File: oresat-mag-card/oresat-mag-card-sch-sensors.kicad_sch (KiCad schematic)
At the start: 22 parts, among them U10 LTC4300A-1, U11 MAX892LEUA+T, U9 ICM-42688-P

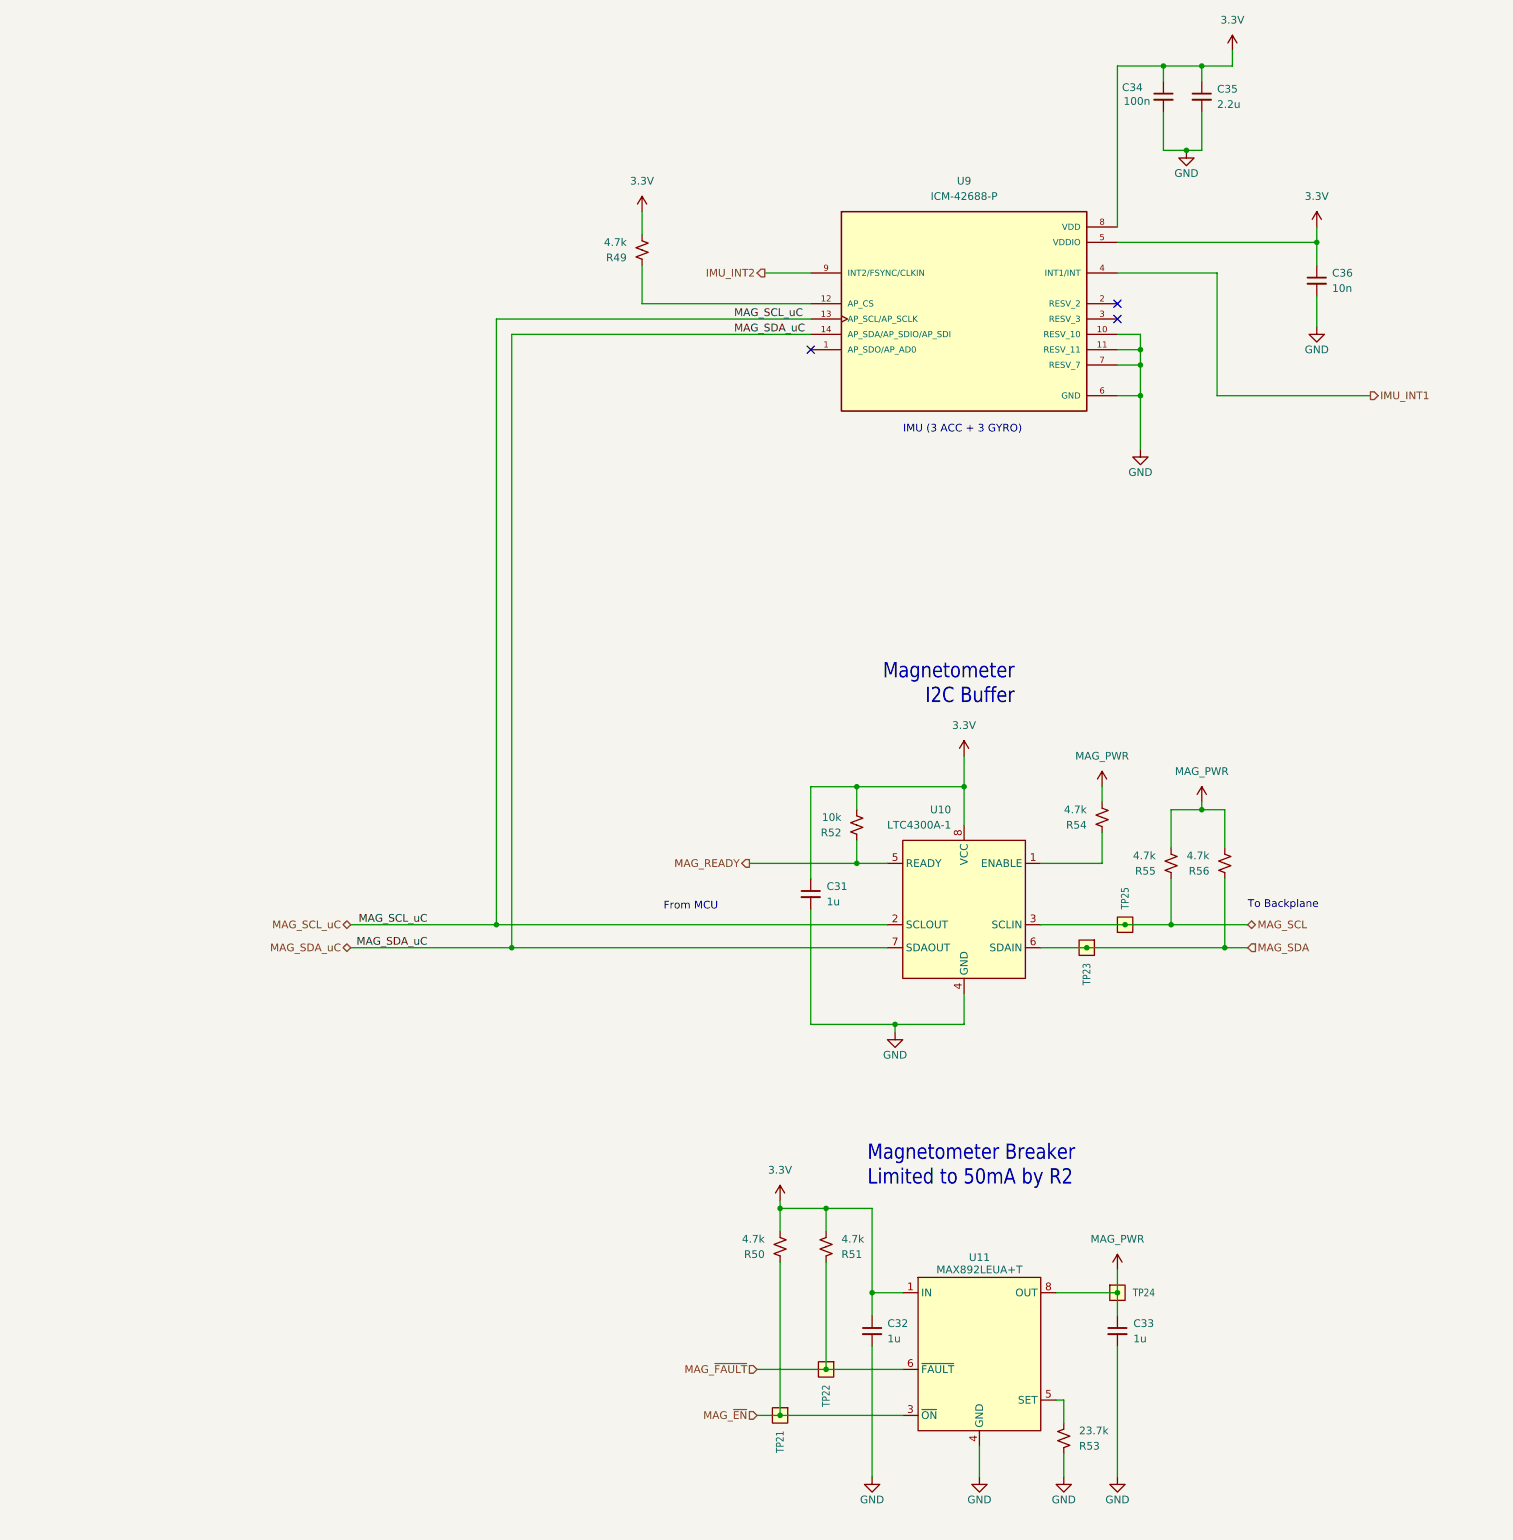
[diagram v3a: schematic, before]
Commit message: Schematic polish, fixed UART TX/RX mixup, imported into layout
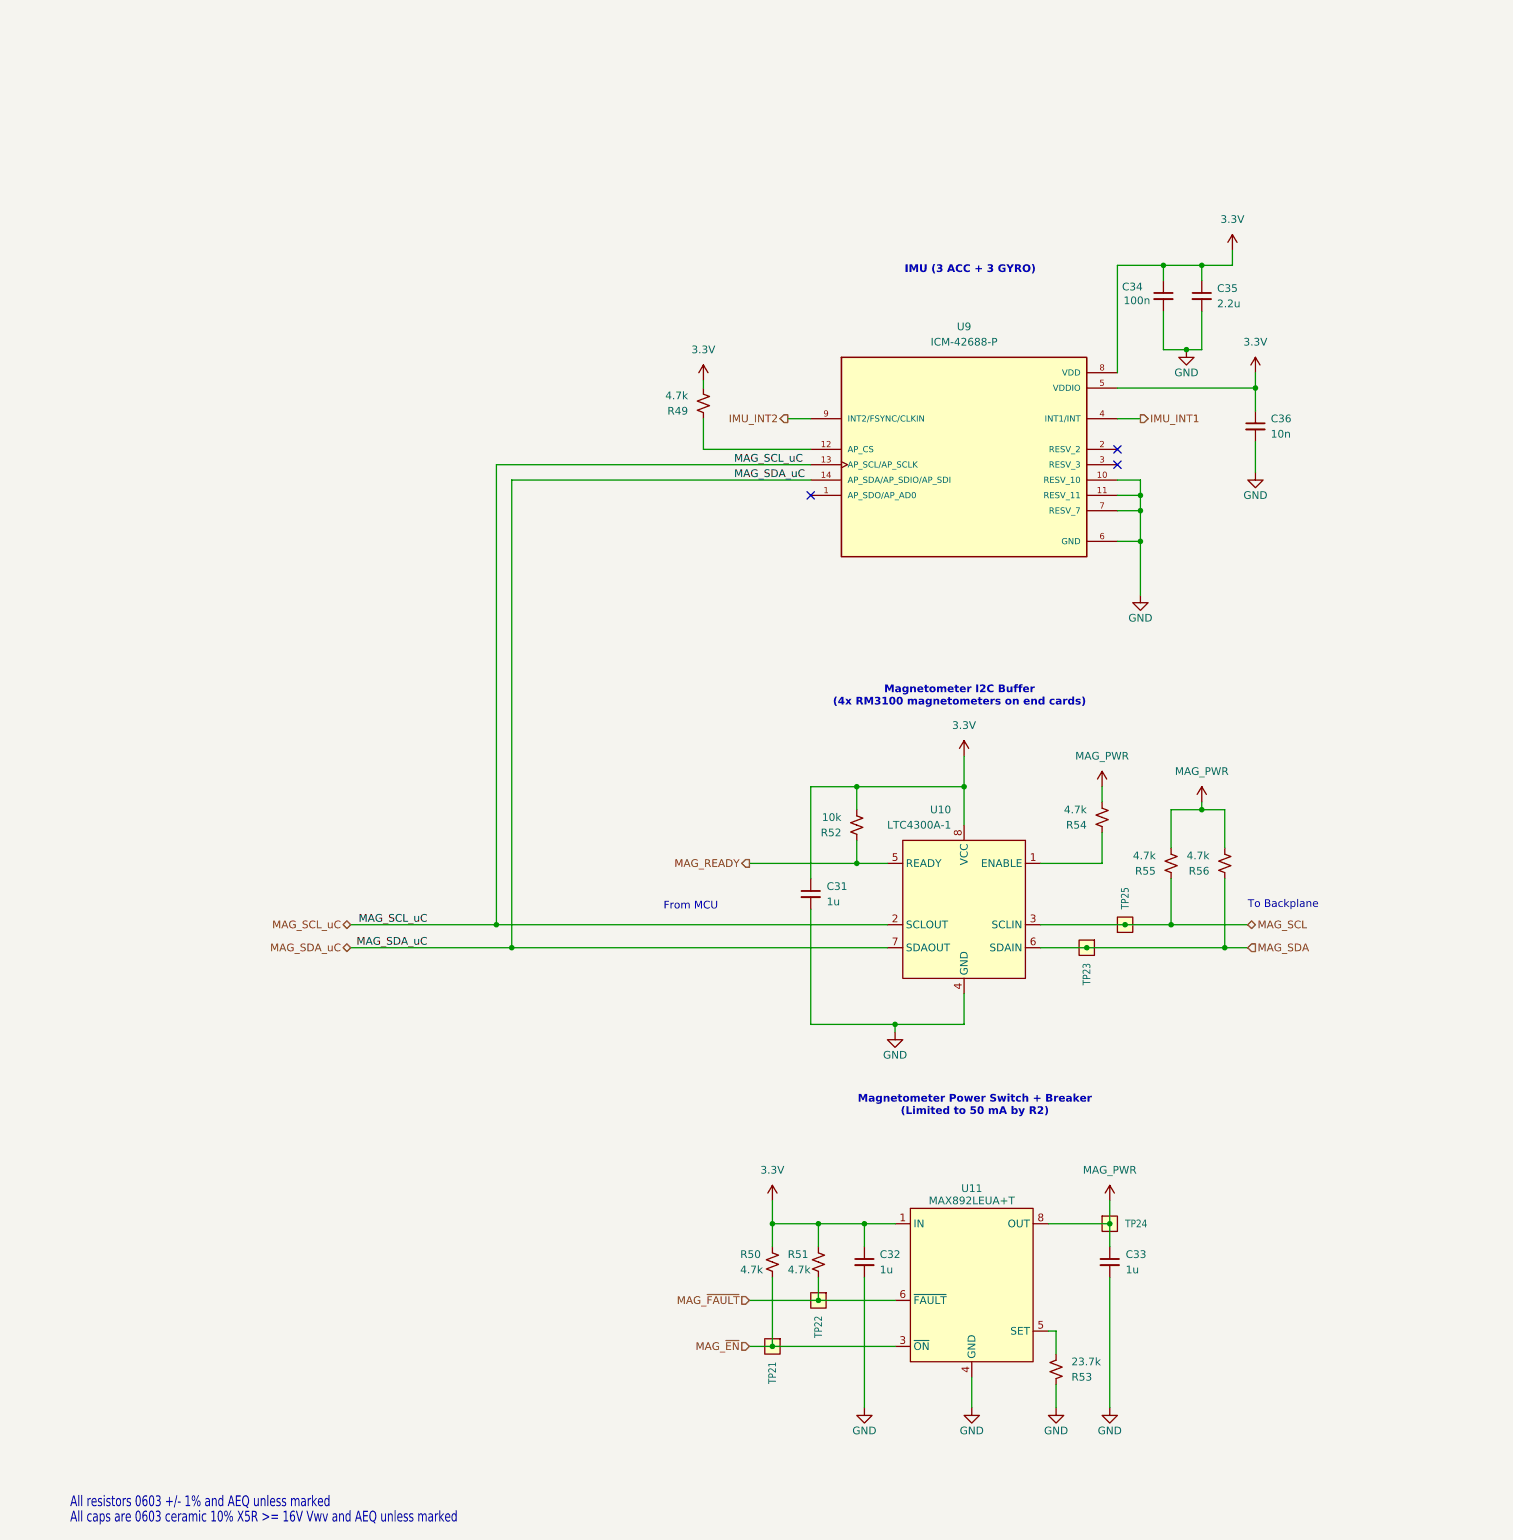
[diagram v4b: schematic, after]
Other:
- note added: "All caps are 0603 ceramic 10% X5R >= 16V Vwv and AEQ unless marked"
- note added: "All resistors 0603 +/- 1% and AEQ unless marked"
- note added: "Magnetometer I2C Buffer (4x RM3100 magnetometers on end cards)"
- note added: "Magnetometer Power Switch + Breaker (Limited to 50 mA by R2)"
- note removed: "Magnetometer Breaker Limited to 50mA by R2"
- note removed: "Magnetometer I2C Buffer"
- company: Edward Tsoi -> Portland State Aerospace Society
- title: Magnetometers + IMU -> OreSat Mag Card
- moved on the sheet: C32, C33, C34, C35, C36, R49, R50, R51, R53, TP21, TP22, TP24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

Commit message: No DRC errors
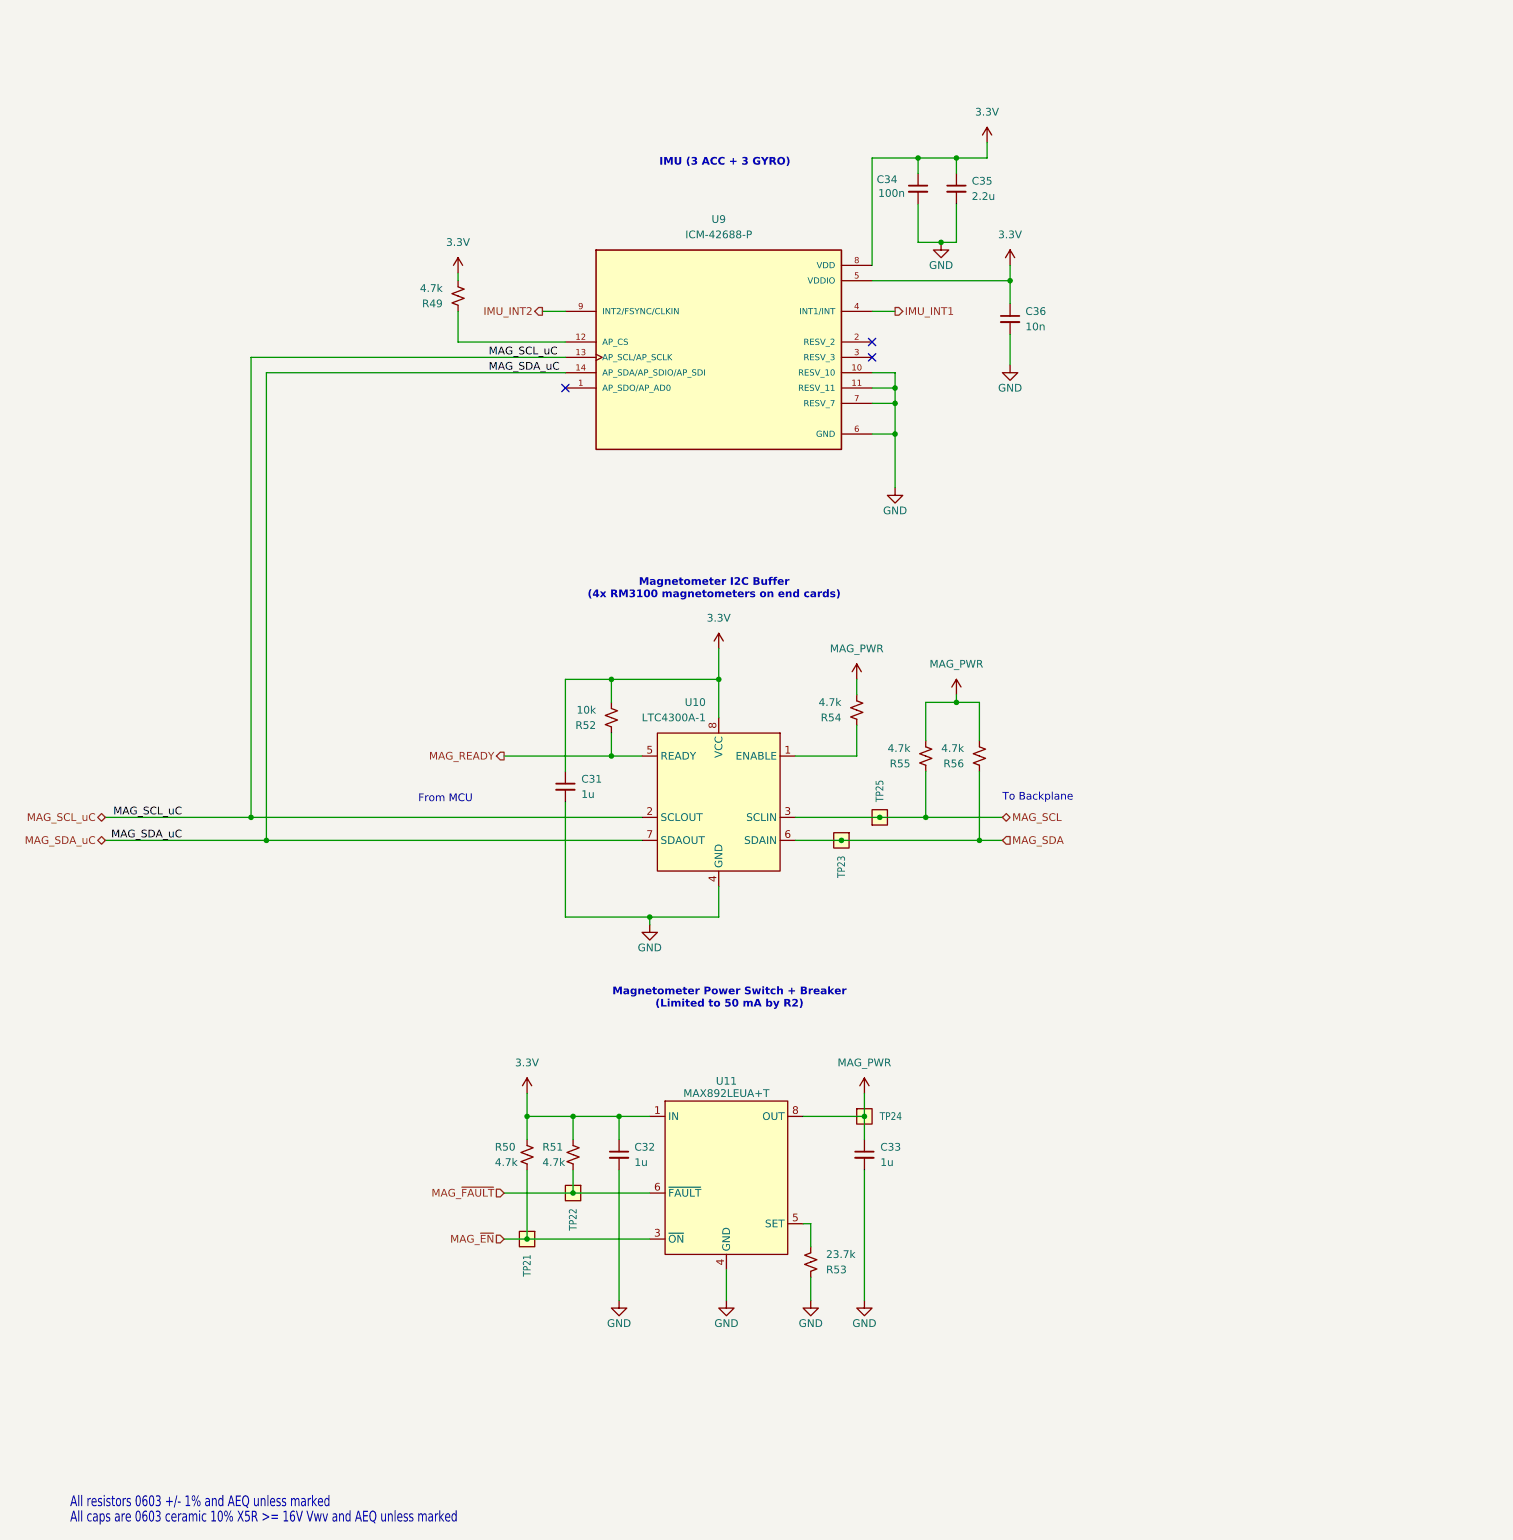
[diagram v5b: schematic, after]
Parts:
- C31, C32, C33, C34, C35, C36, R49, R50, R51, R53, R54, R55, R56: footprint oresat-passives:c_0603-SMALL -> oresat-passives:0603-C-NOSILK
- R52: footprint Resistor_SMD:R_0603_1608Metric -> oresat-passives:0603-C-NOSILK
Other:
- moved on the sheet: C31, C32, C33, C34, C35, C36, R49, R50, R51, R52, R53, R54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

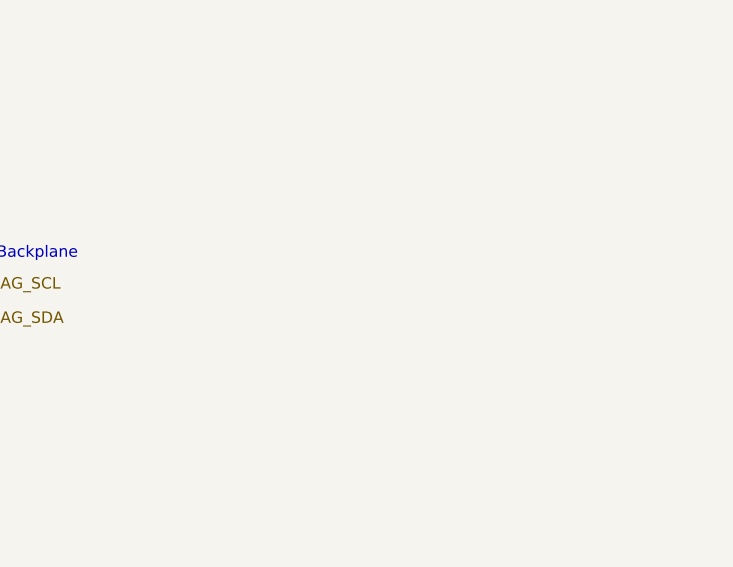
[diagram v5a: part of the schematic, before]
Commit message: Moved to independent MT connectors using pico EZ connectors, and re-laid out the STSPIN250s to be more best-practices.
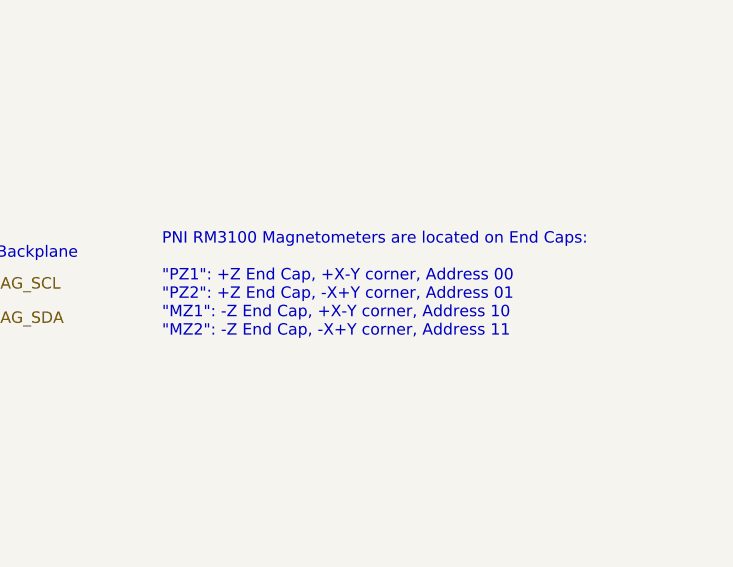
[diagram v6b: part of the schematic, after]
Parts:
- C31, C32, C33: DIST (none) -> DigiKey; DPN (none) -> 490-GRT188R71E105KE13DCT-ND; MFR (none) -> Murata Electronics; MPN (none) -> GRT188R71E105KE13D
- C34: DIST (none) -> DigiKey; DPN (none) -> 399-6856-1-ND; MFR (none) -> KEMET; MPN (none) -> C0603C104K5RACAUTO
- C35: DIST (none) -> DigiKey; DPN (none) -> 490-GRT188C71E225KE13DCT-ND; MFR (none) -> Murata Electronics; MPN (none) -> GRT188C71E225KE13D
- C36: DIST (none) -> DigiKey; DPN (none) -> 399-12983-1-ND; MFR (none) -> KEMET; MPN (none) -> C0603C103J5RACAUTO
- R49, R50, R51, R54, R55, R56: DIST (none) -> DigiKey; DPN (none) -> RMCF0603FT4K70CT-ND; MFR (none) -> Stackpole Electronics; MPN (none) -> RMCF0603FT4K70
- R52: DIST (none) -> DigiKey; DPN (none) -> RMCF0603FT10K0CT-ND; MFR (none) -> Stackpole Electronics; MPN (none) -> RMCF0603FT10K0
- U10: DIST (none) -> DigiKey; DPN (none) -> LTC4300A-1IMS8#TRPBFCT-ND; MFR (none) -> Analog Devices; MPN (none) -> LTC4300A-1IMS8#TRPBF
- U11: DIST (none) -> DigiKey; DPN (none) -> MAX892LEUA+-ND; MFR (none) -> Analog Devices; MPN (none) -> MAX892LEUA+T
- U9: DIST (none) -> DigiKey; DPN (none) -> 1428-ICM-42688-PCT-ND; MFR (none) -> TDK InvenSense; MPN (none) -> ICM-42688-P
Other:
- note added: "PNI RM3100 Magnetometers are located on End Caps: "PZ1": +Z End Cap, +X-Y corner, Address 00 "PZ2": +Z End Cap, -X+Y corner, Address 01 "MZ1": -Z End Cap, +X-Y corner, Address 10 "MZ2": -Z End Cap, -X+Y corner, Address 11"

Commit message: Final mag card
Lots of polishing around best practices layout. Put in giant hole to thread the MTs from below if required for the 3U CubeSats. Cleaned up power layer, added stitching vias, updated readme.
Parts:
- C31, C32, C33, C34, C35, C36, R49, R50, R51, R52, R54, R55, R56: DIS (none) -> DigiKey; DIST DigiKey -> (none)
- U10, U11: footprint oresat-ics:LINEAR-MSOP-8-AND-MAXIM-UMAX-8-21-0036 -> Package_SO:MSOP-8_3x3mm_P0.65mm; DIS (none) -> DigiKey; DIST DigiKey -> (none)
- U9: DIS (none) -> DigiKey; DIST DigiKey -> (none); MANUFACTURER TDK InvenSense -> (none); MAXIMUM_PACKAGE_HEIGHT 0.97mm -> (none); PARTREV 1.2 -> (none)

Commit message: Upgraded to kiCad 10, updated BOM during fabrication woes with Colorodo PCBA, no change in PCB
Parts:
- C31, C32, C33, C34, C35, C36, R49, R50, R51, R52, R54, R55, R56, U10, U11, U9: DIST (none) -> DigiKey
- R53: DIST (none) -> DigiKey; DPN (none) -> RMCF0603FT237RCT-ND; MFR (none) -> Stackpole Electronics Inc; MPN (none) -> RMCF0603FT237R
